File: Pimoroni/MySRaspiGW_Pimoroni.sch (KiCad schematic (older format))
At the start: 5 parts, among them P1 CONN_02X04, U1 NRF24L01

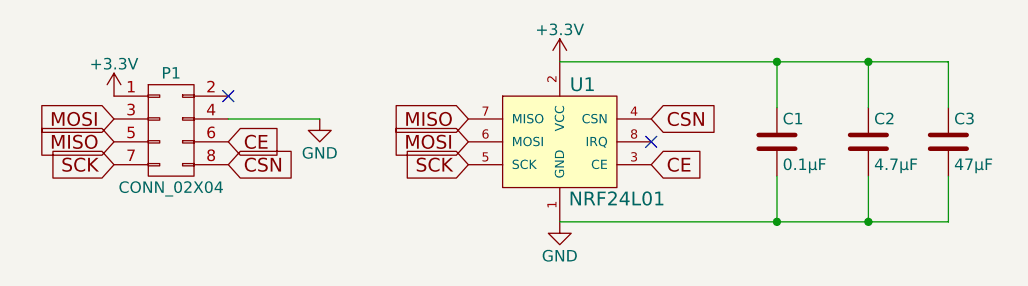
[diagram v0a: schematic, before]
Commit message: v1.1 IRQ support
Added IRQ support on pin 18
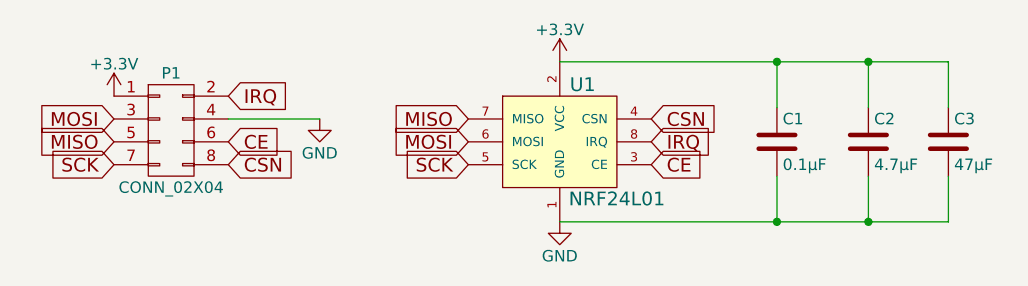
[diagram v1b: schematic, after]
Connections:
- net IRQ: now reaches U1.8 (IRQ)
- net IRQ: now also P1.2 (P2)
- no-connect marks 2 -> 0
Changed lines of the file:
@@
 LIBS:mysensors_security
 LIBS:mysensors_sensors
+LIBS:MySRaspiGW_Pimoroni-cache
 EELAYER 25 0
 EELAYER END
@@
 Sheet 1 1
 Title "MySRaspiGW_Pimoroni"
-Date "05/29/2016"
-Rev "1.0"
+Date "2017-03-13"
+Rev "1.1"
 Comp "https://github.com/emc2cube/MySRaspiGW/tree/master/Pimoroni"
 Comment1 ""
@@
 Connection ~ 4300 1050
 Connection ~ 4700 1050
-NoConn ~ 3750 1400
-NoConn ~ 1900 1200
+Text GLabel 1900 1200 2    60   Input ~ 0
+IRQ
+Text GLabel 3750 1400 2    60   Input ~ 0
+IRQ
 $EndSCHEMATC
